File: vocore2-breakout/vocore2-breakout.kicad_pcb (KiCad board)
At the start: 2 copper layers, 65.5 x 59 mm, 21 parts, among them J1 Conn_01x16_Socket, J2 Conn_01x12_Socket, J3 Conn_01x14_Socket, J4 Conn_01x15_Socket, J5 Conn_02x06_Odd_Even, J6 Conn_02x05_Odd_Even, U1 VOCORE2-SMT

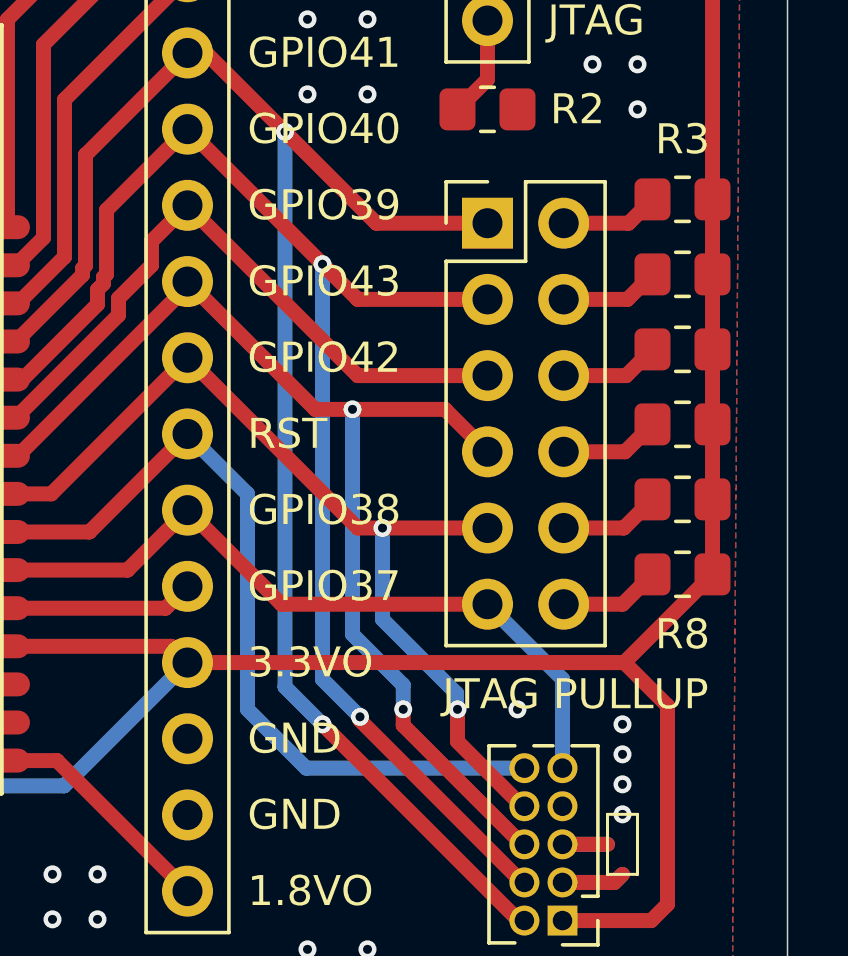
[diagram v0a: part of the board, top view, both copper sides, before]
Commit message: Use correct jtag reset
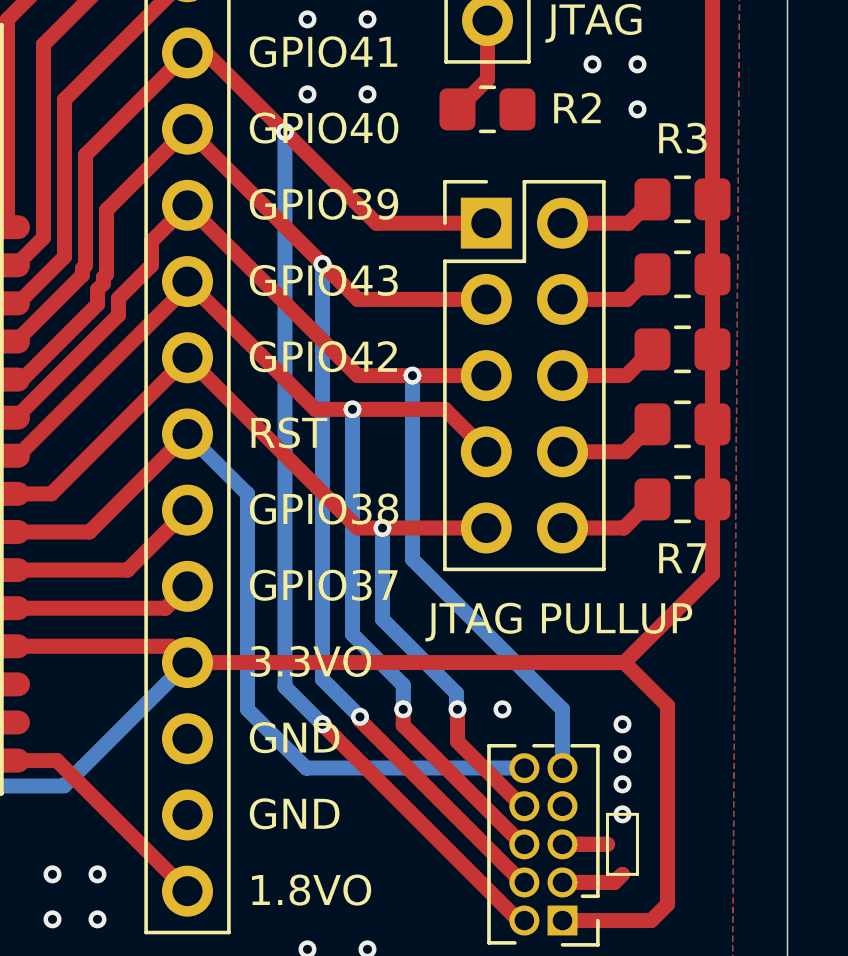
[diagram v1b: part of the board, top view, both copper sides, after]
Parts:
- removed R8: 10K, Resistor_SMD:R_0805_2012Metric_Pad1.20x1.40mm_HandSolder
- removed REF**: OSHW-Symbol_6.7x6mm_SilkScreen, Symbol:OSHW-Symbol_6.7x6mm_SilkScreen
- J5: value Conn_02x06_Odd_Even -> Conn_02x05_Odd_Even; footprint Connector_PinHeader_2.54mm:PinHeader_2x06_P2.54mm_Vertical -> Connector_PinHeader_2.54mm:PinHeader_2x05_P2.54mm_Vertical
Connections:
- J4 pad 10: JTAG_RST -> Net-(J4-Pin_10)
- J4 pad 6: JTAG_RST_N -> JTAG_TRST
- J5 pad 5: JTAG_RST_N -> JTAG_TRST
- J6 pad 9: JTAG_RST -> JTAG_TRST
- U1 pad R10: JTAG_RST -> Net-(J4-Pin_10)
- U1 pad R6: JTAG_RST_N -> JTAG_TRST
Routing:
- net JTAG_TRST: track 0.00 -> 37.7 mm, vias 0 -> 1
- net JTAG_RST: track 25.1 -> 0.00 mm
- net JTAG_RST_N: track 22.6 -> 0.00 mm
- net Net-(J4-Pin_10): track 0.00 -> 7.33 mm
- net Net-(J5-Pin_12): track 3.37 -> 0.00 mm
